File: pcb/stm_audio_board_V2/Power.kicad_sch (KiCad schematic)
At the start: 38 parts, among them U10 TL072, U2 AMS1117-3.3, U4 OP275, U5 AMS1117-3.3, U7 OP275, U8 AMS1117-5.0, U9 L7809

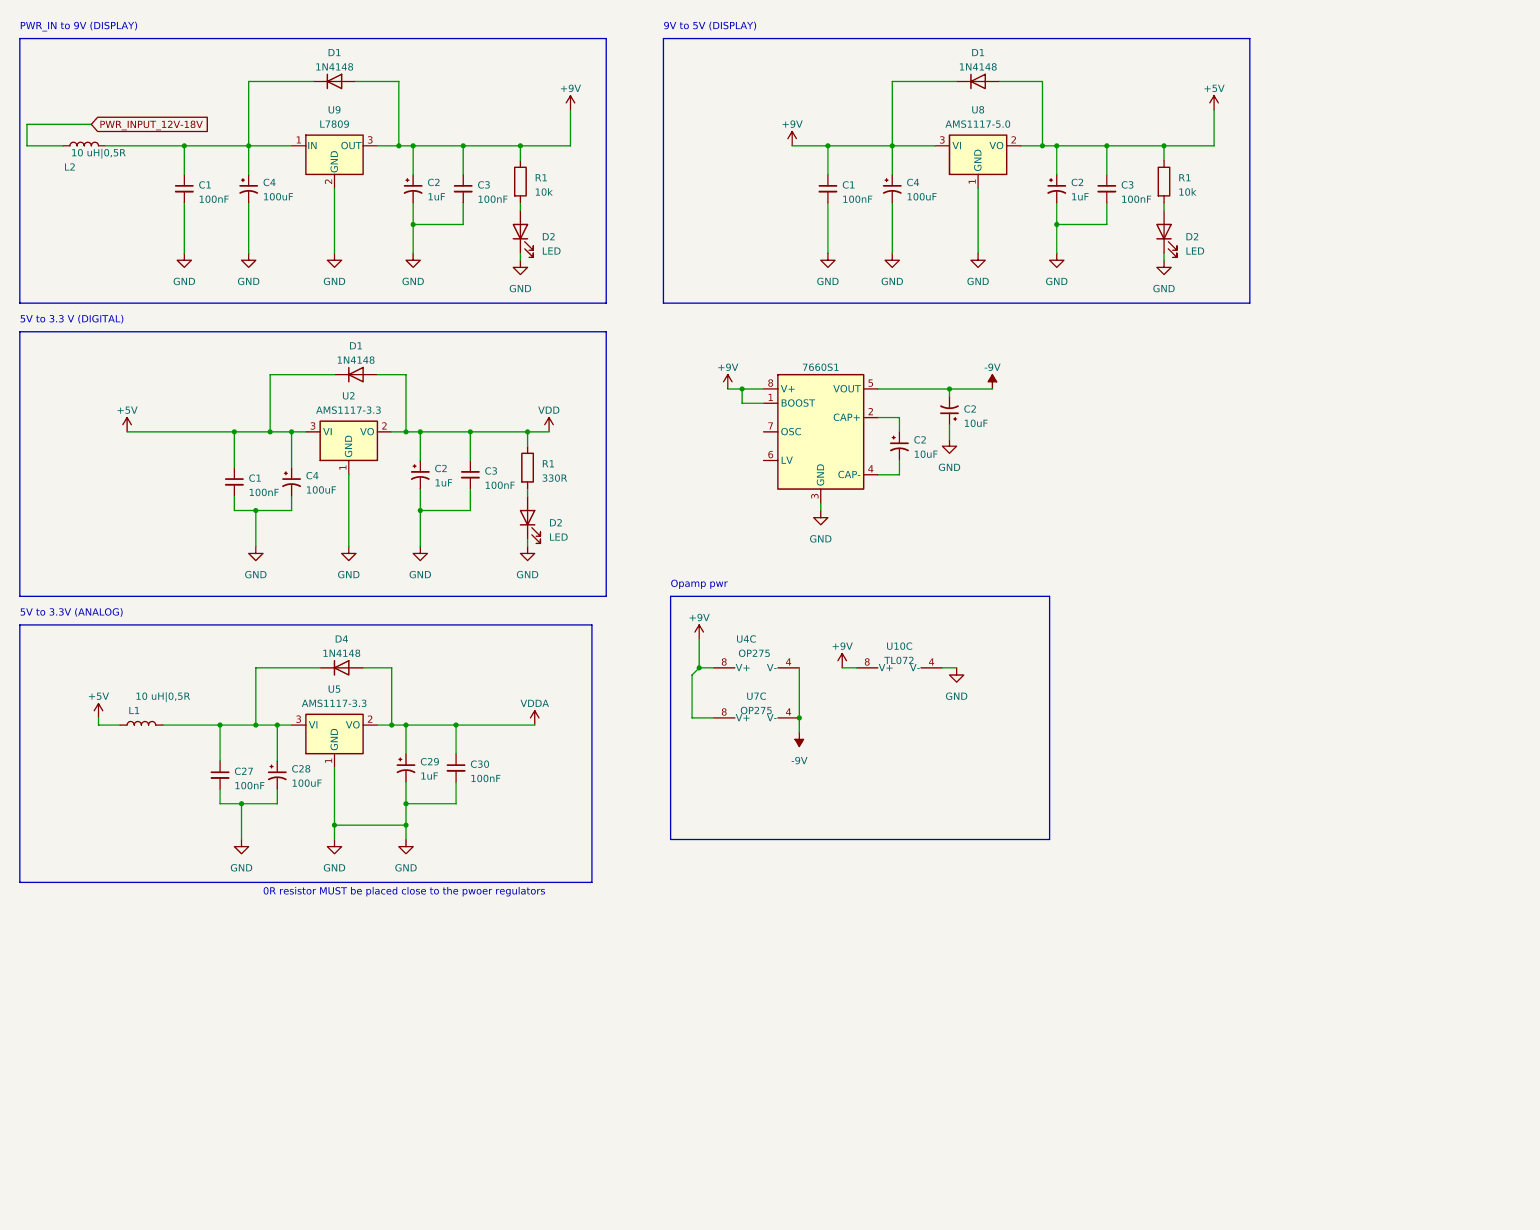
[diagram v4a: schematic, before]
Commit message: ad1939 input stage update
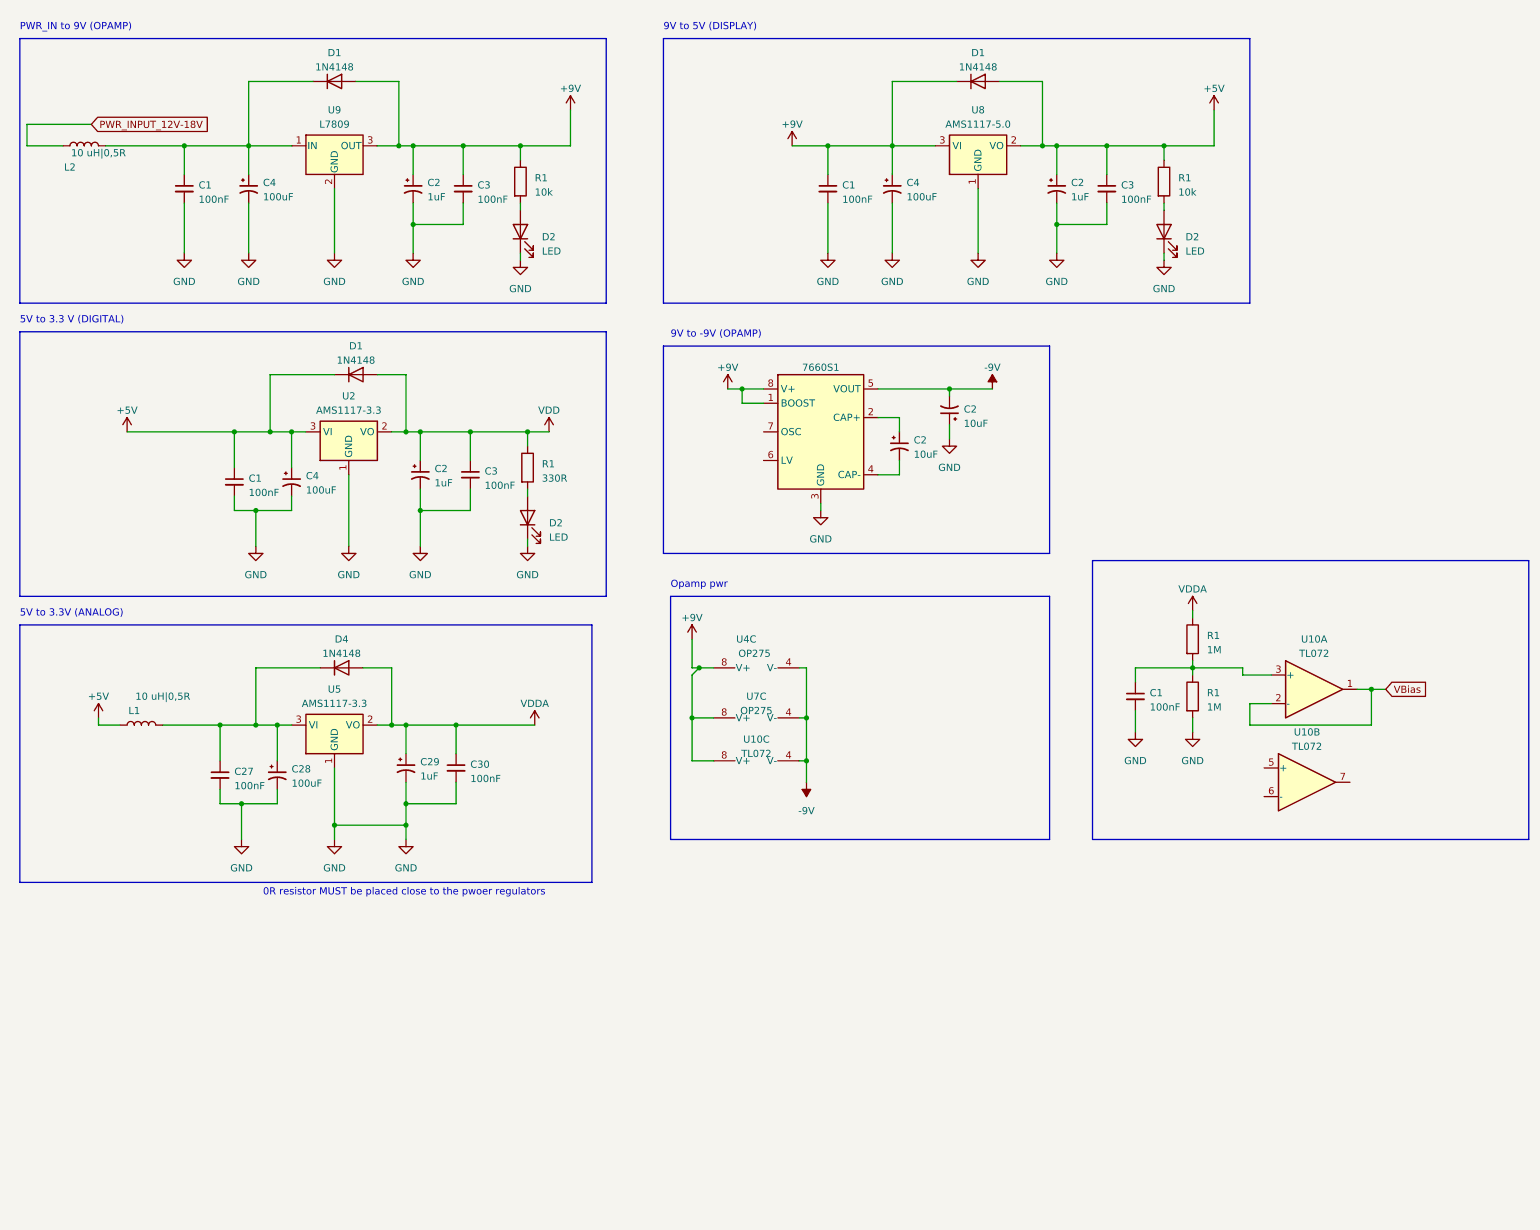
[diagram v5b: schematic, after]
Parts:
- added C1: 100nF, Capacitor_SMD:C_0603_1608Metric_Pad1.08x0.95mm_HandSolder, symbol Device:C_Small
- added R1 (x2): 1M, Resistor_SMD:R_0805_2012Metric_Pad1.20x1.40mm_HandSolder, symbol Device:R
- added unit 1 of U10
- added unit 2 of U10
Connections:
- net -9V: now also U10.4 (V-)
- net GND: now also C1.2, R1.2; no longer U10.4 (V-)
- net VDDA: now also R1.1
- new net: C1.1, R1.1, R1.2, U10.3 (+)
- new net VBias: U10.1, U10.2 (-)
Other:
- note added: "9V to -9V (OPAMP)"
- note added: "PWR_IN to 9V (OPAMP)"
- note removed: "PWR_IN to 9V (DISPLAY)"
- moved on the sheet: U10C

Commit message: ad1939 symbol is finished
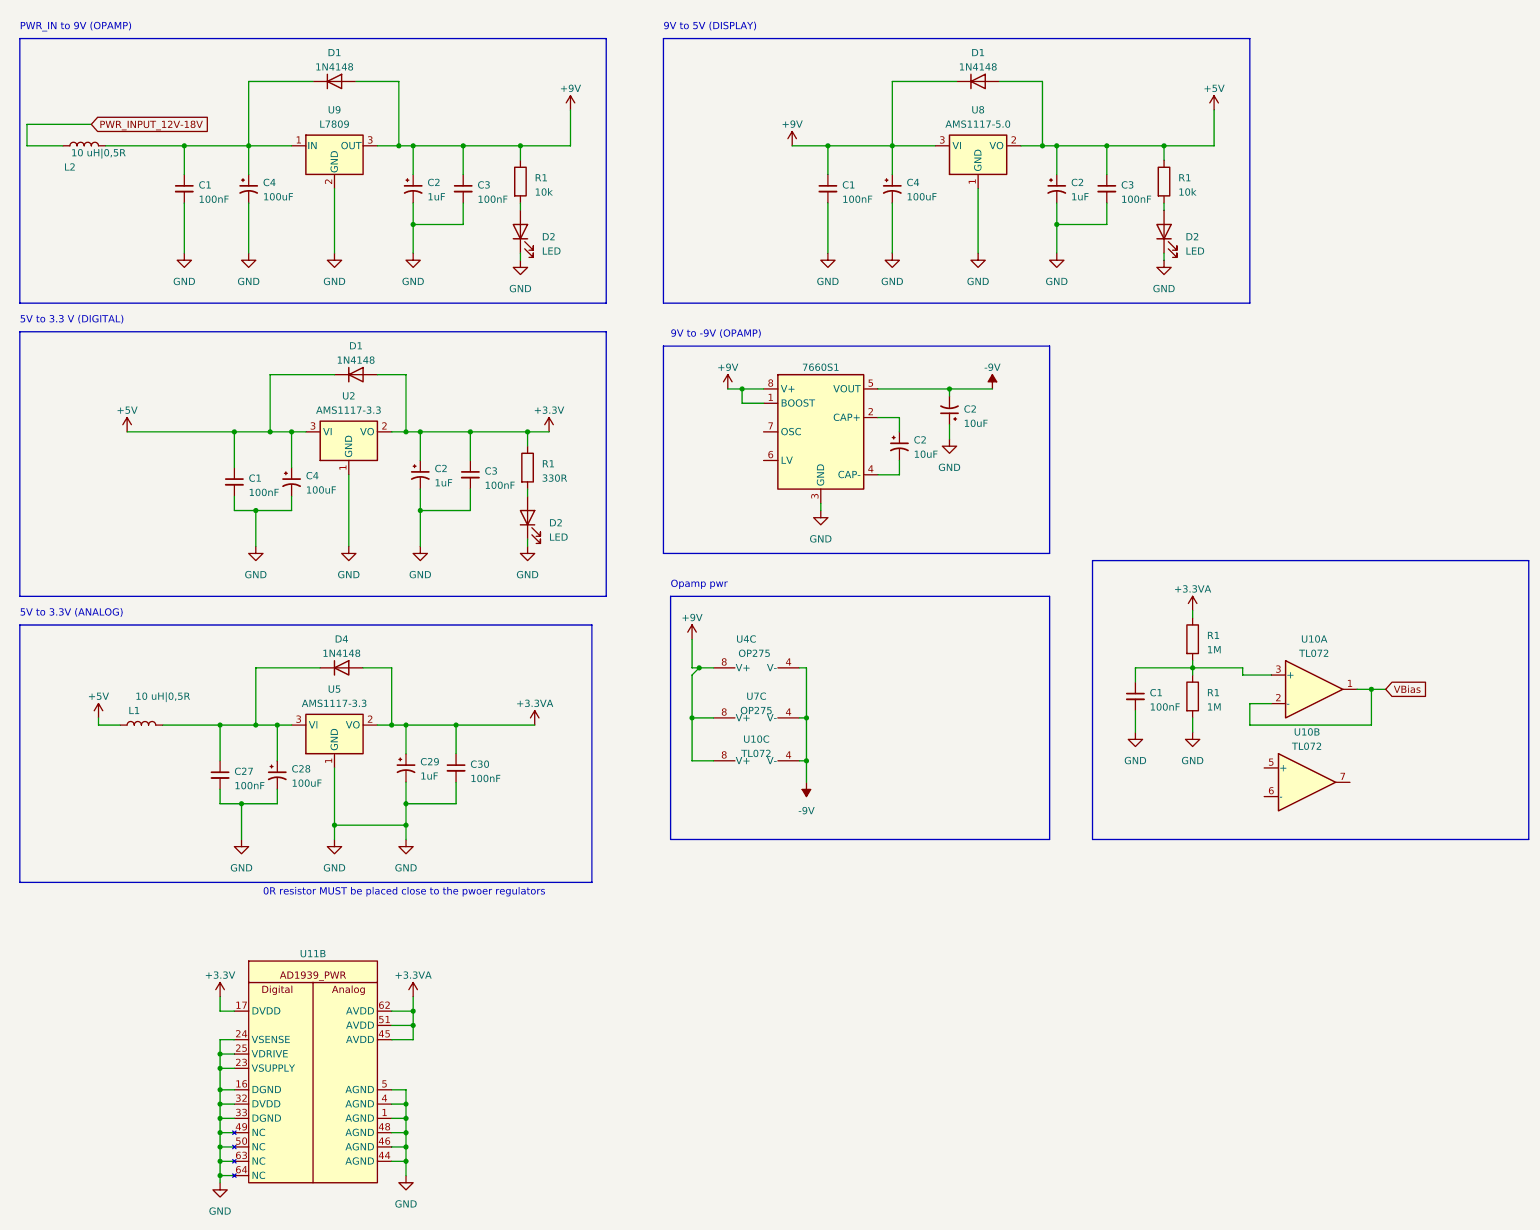
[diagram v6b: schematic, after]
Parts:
- added U11: ~, symbol codec:AD1939
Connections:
- net GND: now also U11.1 (AGND), U11.16 (DGND), U11.23 (VSUPPLY), U11.24 (VSENSE), U11.25 (VDRIVE), U11.32 (DVDD), U11.33 (DGND), U11.4 (AGND), U11.44 (AGND), U11.46 (AGND), U11.48 (AGND), U11.49 (NC), U11.5 (AGND), U11.50 (NC), U11.63 (NC), U11.64 (NC)
- net VDD renamed +3.3V
- net +3.3V: now also U11.17 (DVDD)
- net VDDA renamed +3.3VA
- net +3.3VA: now also U11.45 (AVDD), U11.51 (AVDD), U11.62 (AVDD)
